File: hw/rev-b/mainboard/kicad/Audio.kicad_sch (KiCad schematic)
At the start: 27 parts, among them J21 AUDIO, Q4 SS8050, Q5 SS8050, Q6 SS8050, Q7 SS8550

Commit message: chore(hw): tidy and set ${REVISION} to "B"
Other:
- company: https://is.gd/6hpvh6 -> https://tinyurl.com/econopet-rev-b
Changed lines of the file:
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@@
 	(title_block
 		(title "EconoPET 40/8096")
-		(date "2026-02-27")
-		(rev "B")
-		(company "https://is.gd/6hpvh6")
+		(date "2026-08-25")
+		(rev "${REVISION}")
+		(company "https://tinyurl.com/econopet-rev-b")
 		(comment 1 "Unspecified resistors are 1% / 62.5mW")
 		(comment 2 "Unspecified capacitors are 25V")

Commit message: fix(hw): additional decoupling for audio power rail
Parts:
- added C113: 22u, Capacitor_SMD:C_0805_2012Metric, symbol Device:C_Small
- added C114: 1u, Capacitor_SMD:C_0402_1005Metric, symbol Device:C_Small
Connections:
- net +6V: now also C113.1, C114.1
- net GND: now also C113.2, C114.2

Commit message: chore(hw): create production files
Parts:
- C105: LCSC C1622 -> (none); LCSC Part # (none) -> C1622
- C106, C107, C83: LCSC C307331 -> (none); LCSC Part # (none) -> C307331
- C113: LCSC C45783 -> (none); LCSC Part # (none) -> C45783
- C114, C80: LCSC C52923 -> (none); LCSC Part # (none) -> C52923
- C8, C84: LCSC C96123 -> (none); LCSC Part # (none) -> C96123
- C81: LCSC C1532 -> (none); LCSC Part # (none) -> C1532
- C82: LCSC C31658 -> (none); LCSC Part # (none) -> C31658
- D13, D14: LCSC C2128 -> (none); LCSC Part # (none) -> C2128
- Q4, Q5, Q6: LCSC C2150 -> (none); LCSC Part # (none) -> C2150
- Q7: LCSC C8542 -> (none); LCSC Part # (none) -> C8542
- R36: LCSC C25752 -> (none); LCSC Part # (none) -> C25752
- R37: LCSC C25768 -> (none); LCSC Part # (none) -> C25768
- R67, R69: LCSC C25867 -> (none); LCSC Part # (none) -> C25867
- R68: LCSC C25130 -> (none); LCSC Part # (none) -> C25130
- R70: LCSC C25744 -> (none); LCSC Part # (none) -> C25744
- R71: LCSC C25741 -> (none); LCSC Part # (none) -> C25741
- R72, R73: LCSC C22936 -> (none); LCSC Part # (none) -> C22936
- R74: LCSC C11702 -> (none); LCSC Part # (none) -> C11702

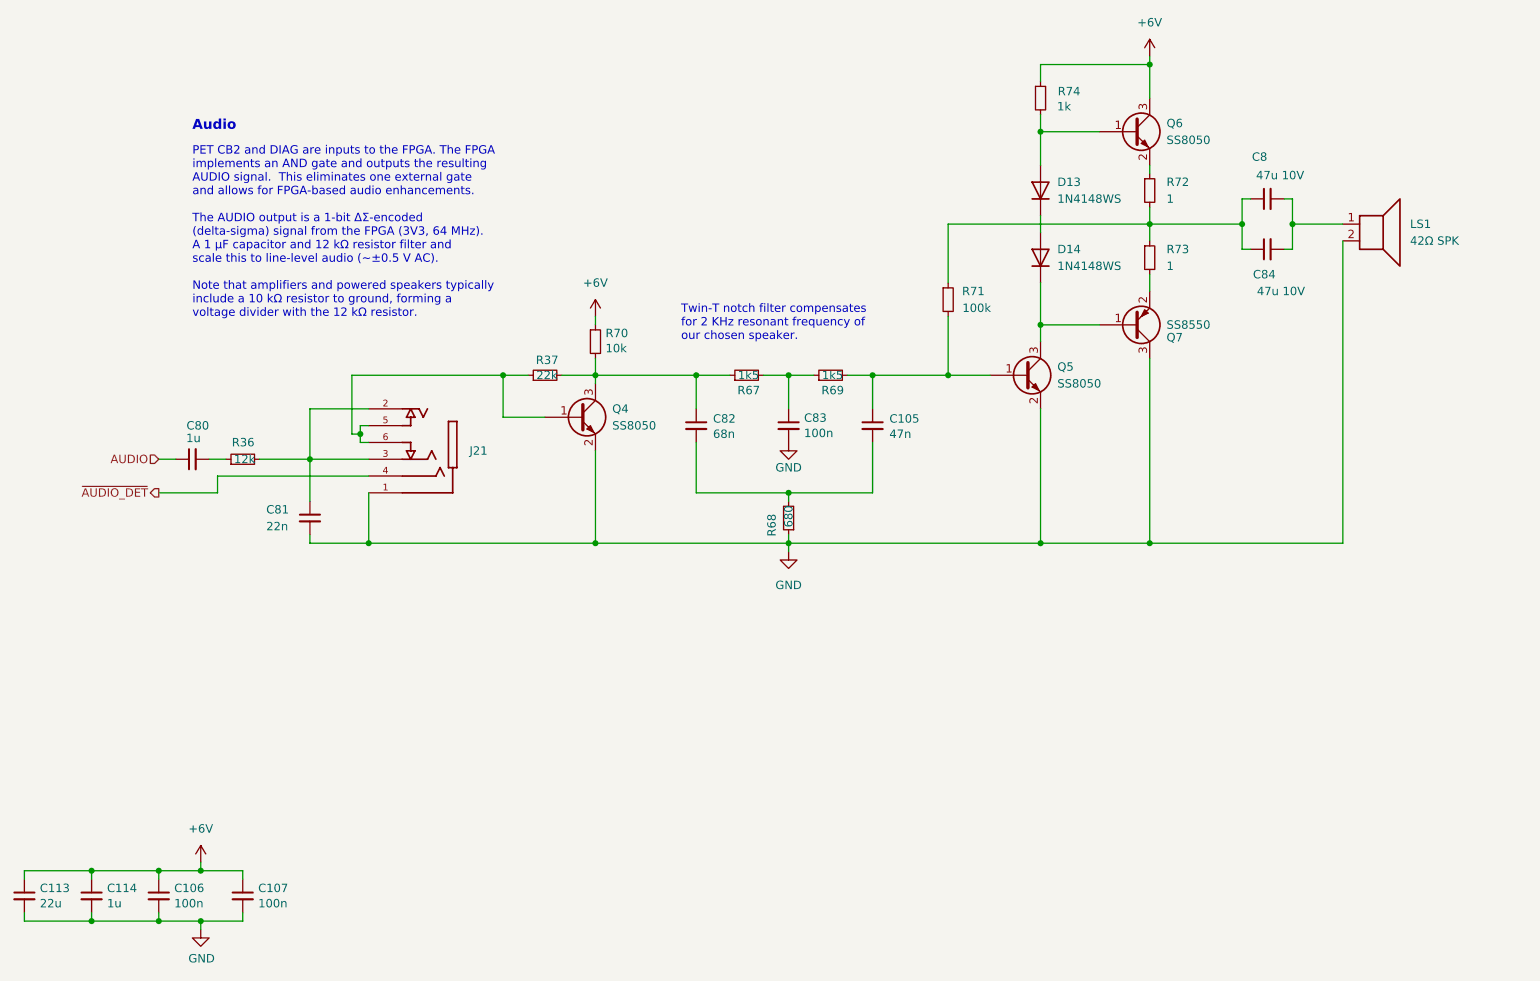
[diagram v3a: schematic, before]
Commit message: feat(hw): separate audio_l / audio_r (schematic only)
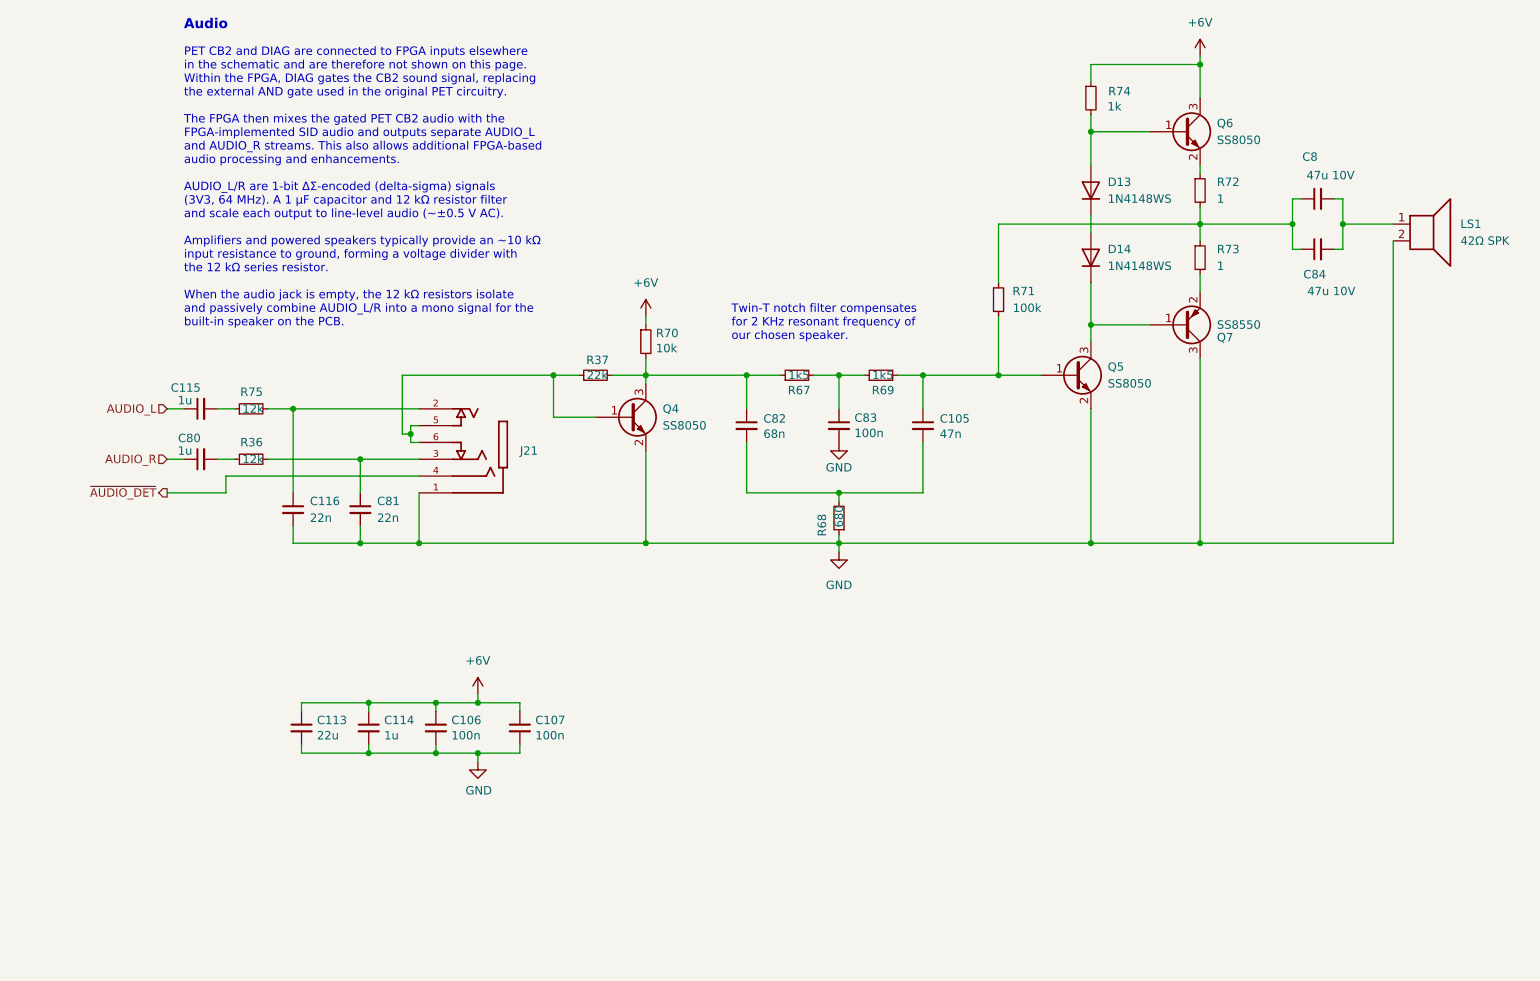
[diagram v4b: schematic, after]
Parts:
- added C115: 1u, Capacitor_SMD:C_0402_1005Metric, symbol Device:C_Small
- added C116: 22n, Capacitor_SMD:C_0402_1005Metric, symbol Device:C_Small
- added R75: 12k, Resistor_SMD:R_0402_1005Metric, symbol Device:R_Small
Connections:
- net GND: now also C116.2
- net at C81.1, J21.3, R36.2: no longer J21.2
- net AUDIO renamed AUDIO_R
- new net: C115.2, R75.1
- new net: C116.1, J21.2, R75.2
- new net AUDIO_L: C115.1
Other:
- note added: "PET CB2 and DIAG are connected to FPGA inputs elsewhere in the schematic and are therefore not shown on this page. Within the FPGA, DIAG gates the CB2 sound signal, replacing the external AND gate used in the original PET circuitry. The FPGA then mixes the gated PET CB2 audio with the FPGA-implemented SID audio and outputs separate AUDIO_L and AUDIO_R streams. This also allows additional FPGA-bas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"
- note removed: "PET CB2 and DIAG are inputs to the FPGA. The FPGA implements an AND gate and outputs the resulting AUDIO signal. This eliminates one external gate and allows for FPGA-based audio enhancements. The AUDIO output is a 1-bit ΔΣ-encoded (delta-sigma) signal from the FPGA (3V3, 64 MHz). A 1 µF capacitor and 12 kΩ resistor filter and scale this to line-level audio (~±0.5 V AC). Note that amplifiers and 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"
- moved on the sheet: C105, C106, C107, C113, C114, C8, C80, C81, C82, C83, C84, D13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
